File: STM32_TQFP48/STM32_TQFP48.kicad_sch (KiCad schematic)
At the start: 92 parts, among them J1 Conn_01x04_Pin, J2 Conn_01x19_Pin, J3 Conn_01x19_Pin, SW1 SW_Push, SW2 SW_Push, U1 STM32L010C6Tx, Y1 Crystal

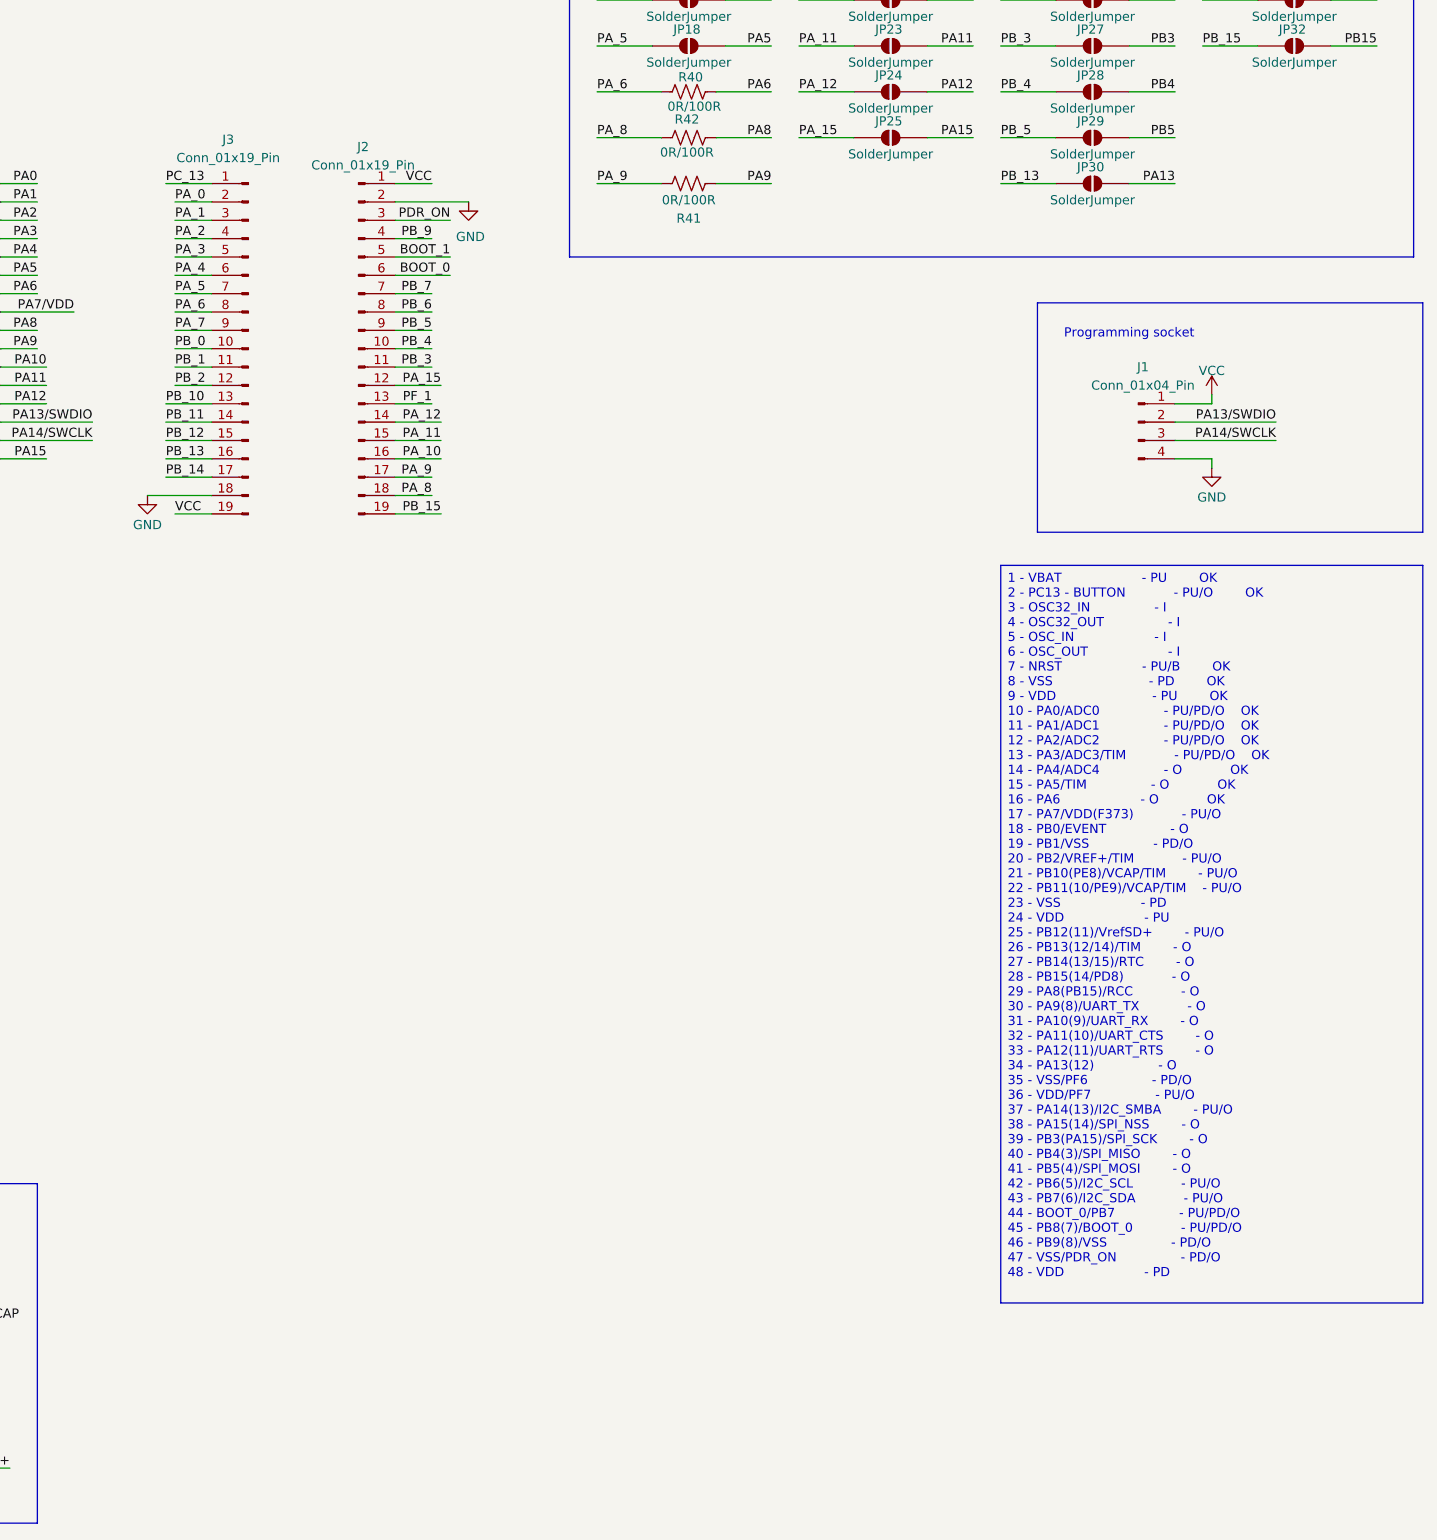
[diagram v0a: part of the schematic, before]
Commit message: STM32_TQFP48(.sch): Reorganizacja wizualna projektu.
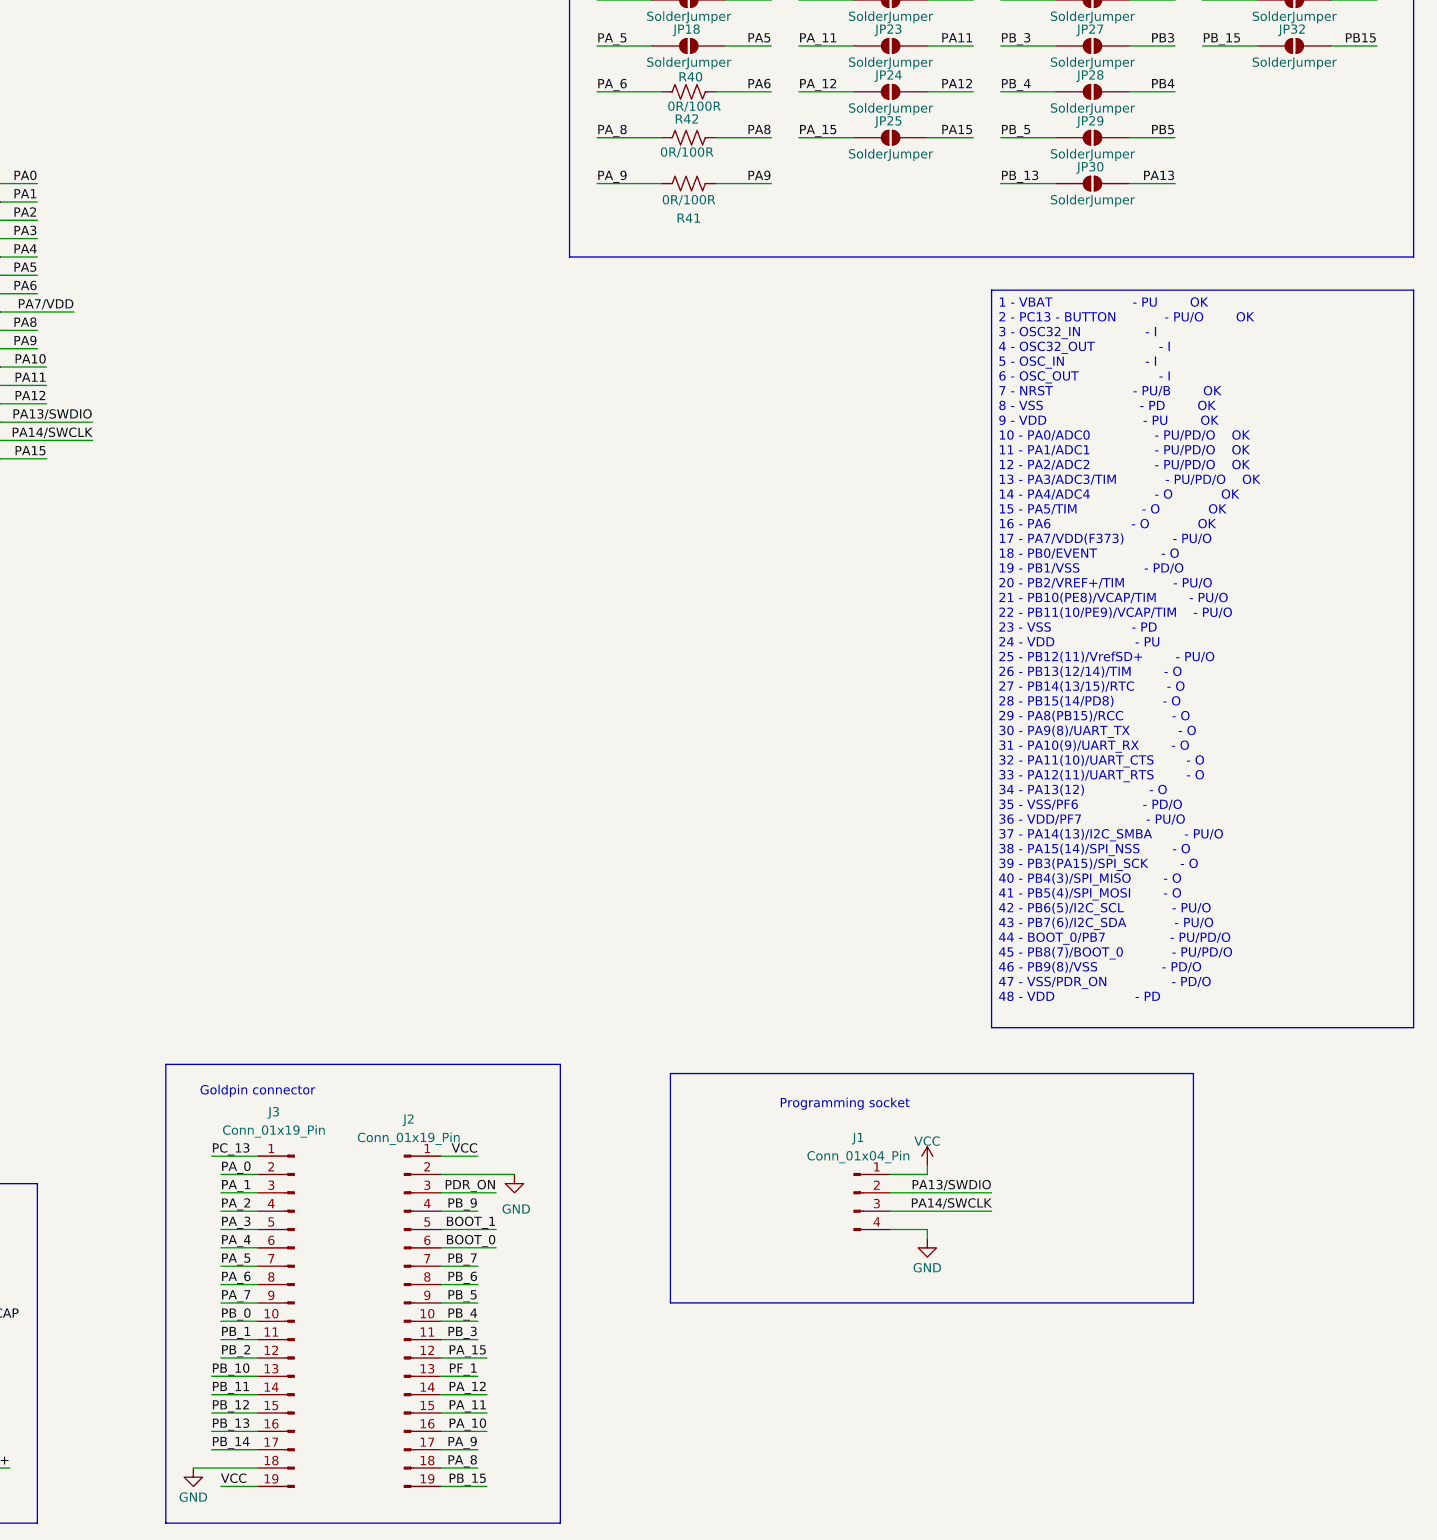
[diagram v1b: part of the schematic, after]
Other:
- note added: "Goldpin connector"
- moved on the sheet: J1, J2, J3

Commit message: STM32_TQFP48(.sch): Wykonanie ERC i poprawa etykiet wskazanych w ERC
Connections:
- net PA13 is gone; now on net PB13: JP30.1 (A)
- net VDD/VCAP0 is gone; now on net PB9/VSS: U1.46 (PB9)
- net PB11/VDD/VCAP: now also JP16.2 (B), R24.2
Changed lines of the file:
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@@
 	)
 	(junction
+		(at 191.77 251.46)
+		(diameter 0)
+		(color 0 0 0 0)
+	)
+	(junction
 		(at 78.74 27.94)
 		(diameter 0)
@@
 	(wire
 		(pts
-			(xy 17.8562 251.46) (xy 26.67 251.46)
-		)
-		(stroke
-			(width 0)
-			(type default)
-		)
-	)
-	(wire
-		(pts
 			(xy 36.83 261.62) (xy 46.99 261.62)
 		)
@@
 	(wire
 		(pts
+			(xy 191.77 251.46) (xy 209.55 251.46)
+		)
+		(stroke
+			(width 0)
+			(type default)
+		)
+	)
+	(wire
+		(pts
 			(xy 163.83 144.78) (xy 176.53 144.78)
 		)
@@
 	(wire
 		(pts
+			(xy 20.32 251.46) (xy 26.67 251.46)
+		)
+		(stroke
+			(width 0)
+			(type default)
+		)
+	)
+	(wire
+		(pts
 			(xy 267.97 274.32) (xy 274.32 274.32)
 		)
@@
 		)
 	)
+	(label "PB9{slash}VSS"
+		(at 163.83 147.32 0)
+		(effects
+			(font
+				(size 1.27 1.27)
+			)
+			(justify left bottom)
+		)
+	)
 	(label "PB_12"
 		(at 173.99 271.78 0)
@@
 		)
 	)
-	(label "VDD{slash}VCAP0"
-		(at 163.83 147.32 0)
-		(effects
-			(font
-				(size 1.27 1.27)
-			)
-			(justify left bottom)
-		)
-	)
 	(label "PA10"
 		(at 213.36 119.38 180)
@@
 		)
 	)
-	(label "PA13"
+	(label "PB13"
 		(at 369.57 93.98 180)
 		(effects
